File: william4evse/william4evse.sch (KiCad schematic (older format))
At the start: 3 parts, among them J1 Boom_Precision_RJ45-B-1x1, U1 RCMB121

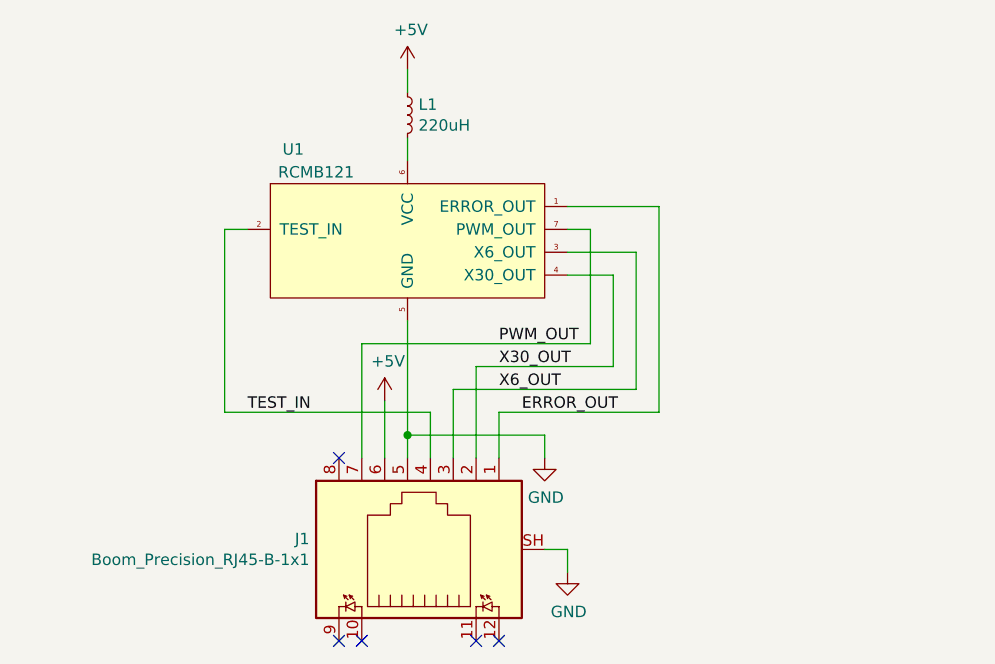
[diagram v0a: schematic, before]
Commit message: william{sch, pcb}: Swap (again) wires
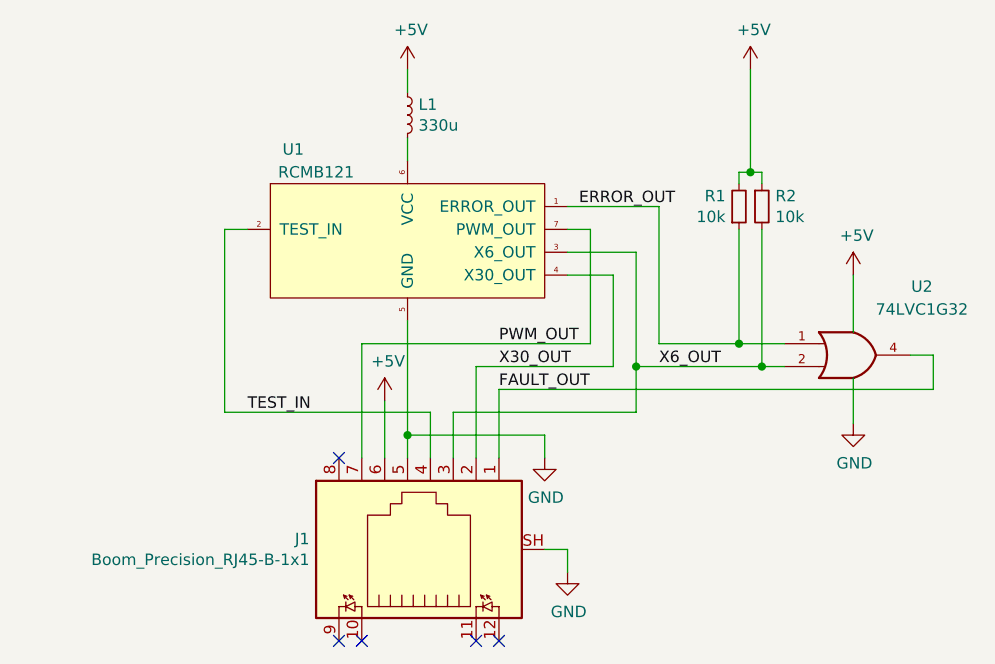
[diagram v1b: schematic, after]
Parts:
- added R1, R2: 10k, Resistor_SMD:R_0603_1608Metric, symbol Device:R_Small
- added U2: 74LVC1G32, Package_TO_SOT_SMD:SOT-353_SC-70-5, symbol 74xGxx:74LVC1G32
- L1: value 220uH -> 330u; LCSC P/N C561744 -> C87557; MFR (none) -> TDK; MFR P/N ALCF362924K561 -> NLCV32T-331K-PF
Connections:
- net +5V: now also R1.2, R2.1, U2.5 (VCC)
- net ERROR_OUT: now also R1.1, U2.1; no longer J1.1
- net GND: now also U2.3 (GND)
- net X6_OUT: now also R2.2, U2.2
- new net FAULT_OUT: J1.1, U2.4
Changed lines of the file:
@@
 	6400 3200 6200 3200
 Wire Wire Line
-	5700 4000 5700 3700
-Wire Wire Line
-	5700 3700 6500 3700
-Wire Wire Line
-	6500 3700 6500 3100
+	5900 4000 5900 3700
 Wire Wire Line
 	6500 3100 6200 3100
@@
 Wire Wire Line
 	4700 3000 4800 3000
-Wire Wire Line
-	5900 4000 5900 3800
-Wire Wire Line
-	5900 3800 6600 3800
-Wire Wire Line
-	6600 3800 6600 2900
 Wire Wire Line
 	6600 2900 6200 2900
@@
 Text Label 5900 3600 0    50   ~ 0
 X30_OUT
-Text Label 5900 3700 0    50   ~ 0
+Text Label 6600 3600 0    50   ~ 0
 X6_OUT
-Text Label 6000 3800 0    50   ~ 0
+Text Label 6250 2900 0    50   ~ 0
 ERROR_OUT
 Wire Wire Line
@@
 P 5500 2500
 F 0 "L1" H 5548 2546 50  0000 L CNN
-F 1 "220uH" H 5548 2455 50  0000 L CNN
+F 1 "330u" H 5548 2455 50  0000 L CNN
 F 2 "Inductor_SMD:L_1210_3225Metric" H 5500 2500 50  0001 C CNN
-F 3 "~" H 5500 2500 50  0001 C CNN
-F 4 "C561744" H 5500 2500 50  0001 C CNN "LCSC P/N"
-F 5 "ALCF362924K561" H 5500 2500 50  0001 C CNN "MFR P/N"
+F 3 "https://datasheet.lcsc.com/lcsc/1810201211_TDK-NLCV32T-331K-PF_C87557.pdf" H 5500 2500 50  0001 C CNN
+F 4 "C87557" H 5500 2500 50  0001 C CNN "LCSC P/N"
+F 5 "NLCV32T-331K-PF" H 5500 2500 50  0001 C CNN "MFR P/N"
+F 6 "TDK" H 5500 2500 50  0001 C CNN "MFR"
 	1    5500 2500
 	1    0    0    -1
@@
 Wire Wire Line
 	5500 2400 5500 2300
+Wire Wire Line
+	5700 3800 5700 4000
+$Comp
+L 74xGxx:74LVC1G32 U2
+U 1 1 60B56C17
+P 7450 3550
+F 0 "U2" H 7750 3850 50  0000 C CNN
+F 1 "74LVC1G32" H 7750 3750 50  0000 C CNN
+F 2 "Package_TO_SOT_SMD:SOT-353_SC-70-5" H 7450 3550 50  0001 C CNN
+F 3 "http://www.ti.com/lit/sg/scyt129e/scyt129e.pdf" H 7450 3550 50  0001 C CNN
+F 4 "C12516" H 7450 3550 50  0001 C CNN "LCSC P/N"
+F 5 "Nexperia" H 7450 3550 50  0001 C CNN "MFR"
+F 6 "74LVC1G32GW,125" H 7450 3550 50  0001 C CNN "MFR P/N"
+	1    7450 3550
+	1    0    0    -1
+$EndComp
+Wire Wire Line
+	6600 2900 6600 3500
+Wire Wire Line
+	6600 3500 6950 3500
+Wire Wire Line
+	6500 3100 6500 3600
+Wire Wire Line
+	6500 3600 7050 3600
+Wire Wire Line
+	7700 3550 7800 3550
+Wire Wire Line
+	7800 3550 7800 3700
+Wire Wire Line
+	5900 3700 7800 3700
+Text Label 5900 3700 0    50   ~ 0
+FAULT_OUT
+Wire Wire Line
+	5700 3800 6500 3800
+Wire Wire Line
+	6500 3800 6500 3600
+Connection ~ 6500 3600
+$Comp
+L Device:R_Small R1
+U 1 1 60B5E628
+P 6950 2900
+F 0 "R1" H 6891 2854 50  0000 R CNN
+F 1 "10k" H 6891 2945 50  0000 R CNN
+F 2 "Resistor_SMD:R_0603_1608Metric" H 6950 2900 50  0001 C CNN
+F 3 "https://datasheet.lcsc.com/szlcsc/Uniroyal-Elec-0603WAF1002T5E_C25804.pdf" H 6950 2900 50  0001 C CNN
+F 4 "C25804" H 6950 2900 50  0001 C CNN "LCSC P/N"
+F 5 "Uniroyal Elec" H 6950 2900 50  0001 C CNN "MFR"
+F 6 "0603WAF1002T5E" H 6950 2900 50  0001 C CNN "MFR P/N"
+	1    6950 2900
+	1    0    0    1
+$EndComp
+$Comp
+L Device:R_Small R2
+U 1 1 60B6145F
+P 7050 2900
+F 0 "R2" H 7109 2946 50  0000 L CNN
+F 1 "10k" H 7109 2855 50  0000 L CNN
+F 2 "Resistor_SMD:R_0603_1608Metric" H 7050 2900 50  0001 C CNN
+F 3 "https://datasheet.lcsc.com/szlcsc/Uniroyal-Elec-0603WAF1002T5E_C25804.pdf" H 7050 2900 50  0001 C CNN
+F 4 "C25804" H 7050 2900 50  0001 C CNN "LCSC P/N"
+F 5 "Uniroyal Elec" H 7050 2900 50  0001 C CNN "MFR"
+F 6 "0603WAF1002T5E" H 7050 2900 50  0001 C CNN "MFR P/N"
+	1    7050 2900
+	1    0    0    -1
+$EndComp
+Wire Wire Line
+	6950 3000 6950 3500
+Connection ~ 6950 3500
+$Comp
+L power:+5V #PWR0101
+U 1 1 60B646F5
+P 7000 2300
+F 0 "#PWR0101" H 7000 2150 50  0001 C CNN
+F 1 "+5V" H 7015 2473 50  0000 C CNN
+F 2 "" H 7000 2300 50  0001 C CNN
+F 3 "" H 7000 2300 50  0001 C CNN
+	1    7000 2300
+	1    0    0    -1
+$EndComp
+Wire Wire Line
+	6950 2800 6950 2750
+Wire Wire Line
+	6950 2750 7000 2750
+Wire Wire Line
+	7050 2750 7050 2800
+Wire Wire Line
+	7000 2750 7000 2300
+Connection ~ 7000 2750
+Wire Wire Line
+	7000 2750 7050 2750
+Wire Wire Line
+	6950 3500 7150 3500
+Wire Wire Line
+	7050 3000 7050 3600
+Connection ~ 7050 3600
+Wire Wire Line
+	7050 3600 7150 3600
+$Comp
+L power:+5V #PWR0102
+U 1 1 60B6705A
+P 7450 3200
+F 0 "#PWR0102" H 7450 3050 50  0001 C CNN
+F 1 "+5V" H 7465 3373 50  0000 C CNN
+F 2 "" H 7450 3200 50  0001 C CNN
+F 3 "" H 7450 3200 50  0001 C CNN
+	1    7450 3200
+	1    0    0    -1
+$EndComp
+Wire Wire Line
+	7450 3200 7450 3450
+Wire Wire Line
+	7450 3650 7450 3850
+$Comp
+L power:GND #PWR0103
+U 1 1 60B69540
+P 7450 3850
+F 0 "#PWR0103" H 7450 3600 50  0001 C CNN
+F 1 "GND" H 7455 3677 50  0000 C CNN
+F 2 "" H 7450 3850 50  0001 C CNN
+F 3 "" H 7450 3850 50  0001 C CNN
+	1    7450 3850
+	1    0    0    -1
+$EndComp
 $EndSCHEMATC
